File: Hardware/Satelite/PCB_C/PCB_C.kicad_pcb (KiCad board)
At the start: 2 copper layers, 54 x 54 mm, 54 parts, among them IC4 MS563702BA03-50, IC5 BMX055, J1 SWD, J3 Conector_PCB_B-C, J4 Conector_Expansion_CanSat, J5 USB_B_Micro, M1 Spacer, M2 Spacer, M3 Spacer, U1 TXS0104ERGYR, U2 TCA9802DGKR, U3 W25Q32JVSSIQ, U4 TXS0104ERGYR, U5 BL654, U6 Si7006-A20-IM1, U7 Si7051-A20, Y1 LFXTAL016178

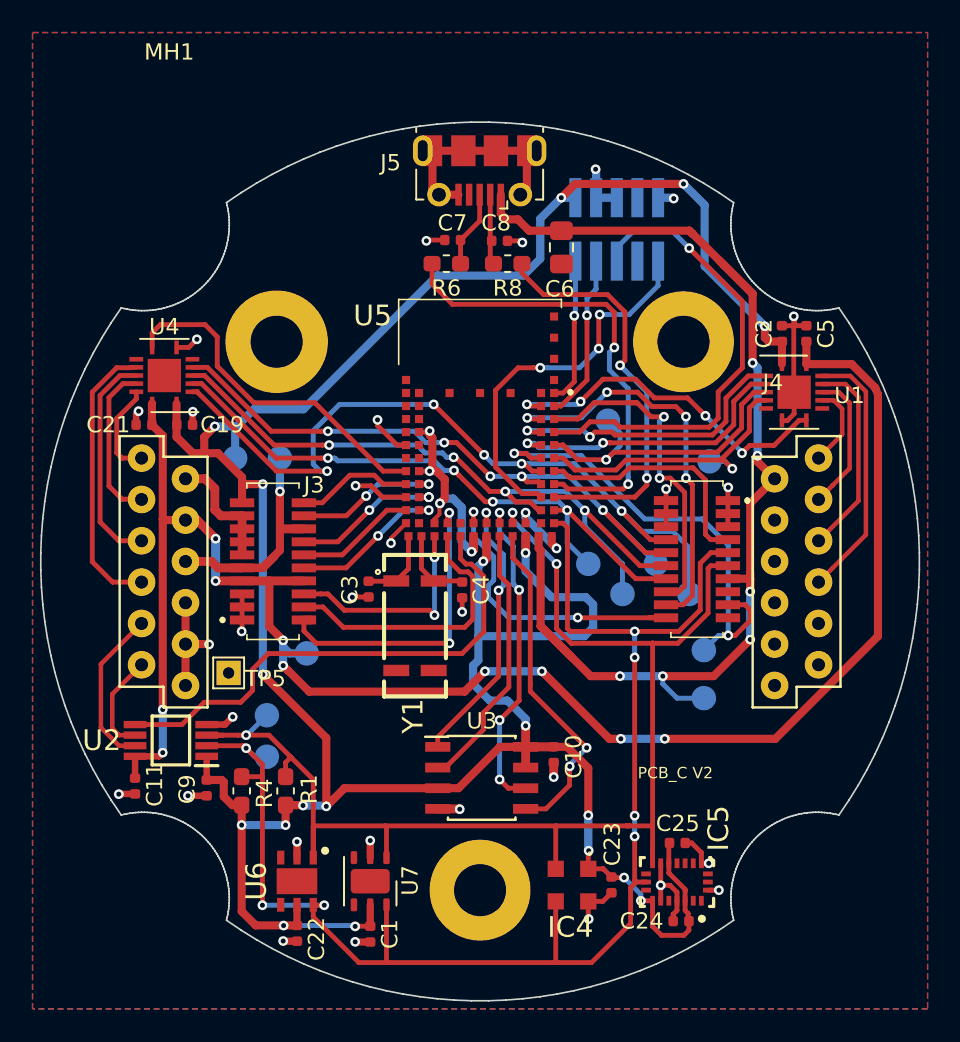
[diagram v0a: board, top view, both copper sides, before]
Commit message: Pequeñas mejoras a PCB_C
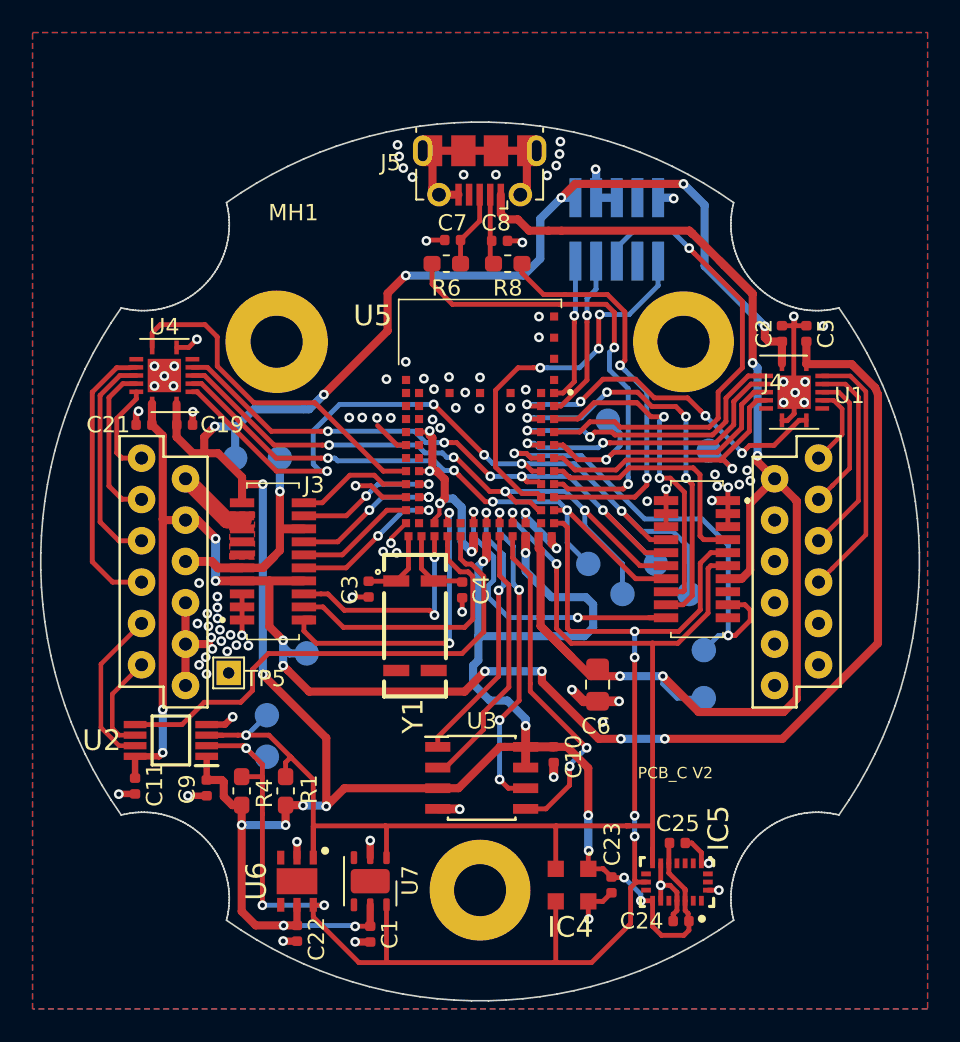
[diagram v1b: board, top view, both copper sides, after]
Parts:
- moved C6 27.0 mm to (17.2, 17.6)
- moved TP10 0.65 mm to (24.1, 3.20)
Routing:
- net VBUS: track 73.4 -> 85.5 mm, vias 6 -> 4
- net +BATT: track 7.58 -> 4.63 mm
- net GND: track 94.0 -> 96.9 mm, vias 36 -> 104
- net +3V3_Internal: track 191.7 -> 193.1 mm, vias 19 -> 21
- net +3V3: track 128.4 -> 129.0 mm
- added copper zone on F.Cu, net +BATT

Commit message: Agregado de modelos 3D a PCB_C
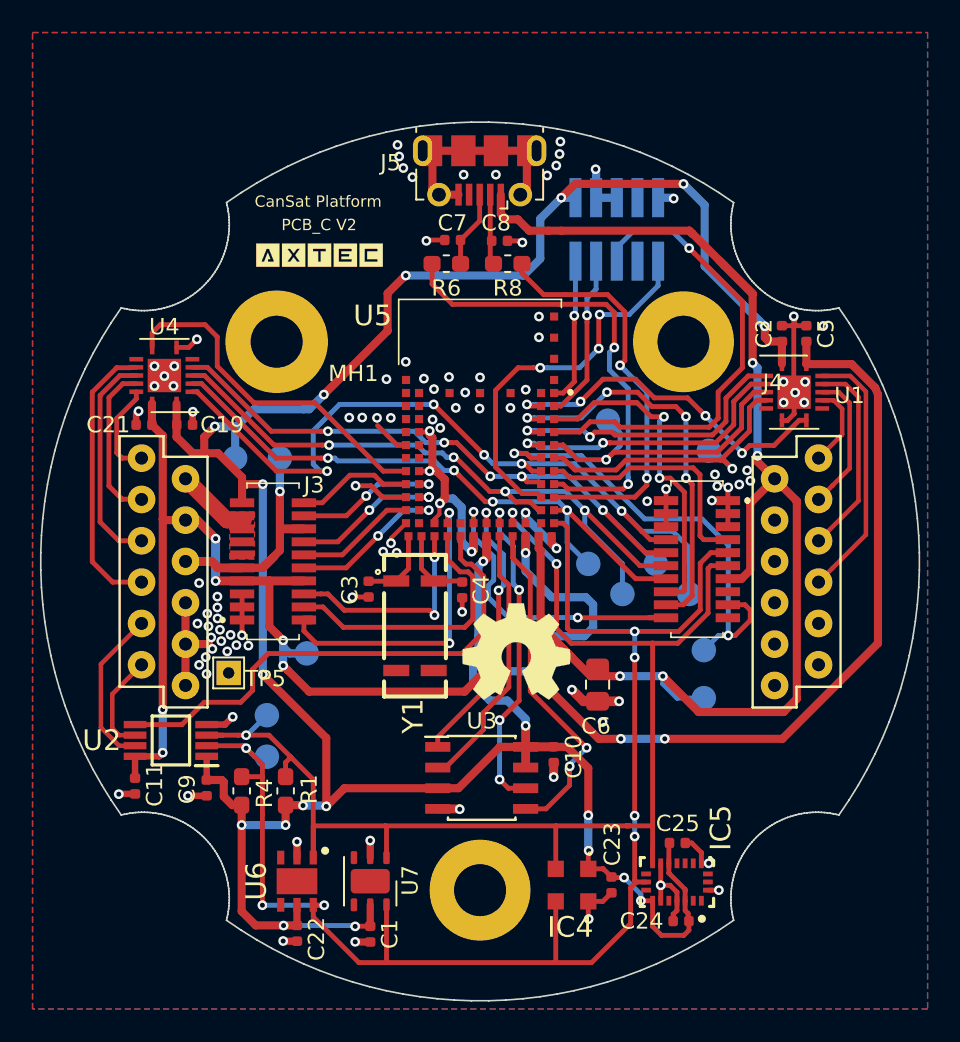
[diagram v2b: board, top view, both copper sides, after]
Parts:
- added G***: LOGO, AXTEC:Logo_AXTEC, B.Cu at (0.05, -9.02)
- added G***: LOGO, AXTEC:Logo_AXTEC, F.Cu at (0.20, -9.02)
- added REF**: OSHW-Symbol_6.7x6mm_SilkScreen, Symbol:OSHW-Symbol_6.7x6mm_SilkScreen, B.Cu at (12.2, 15.5)
- added REF**: OSHW-Symbol_6.7x6mm_SilkScreen, Symbol:OSHW-Symbol_6.7x6mm_SilkScreen, F.Cu at (12.2, 15.5)
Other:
- board text added: "CanSat Platform"

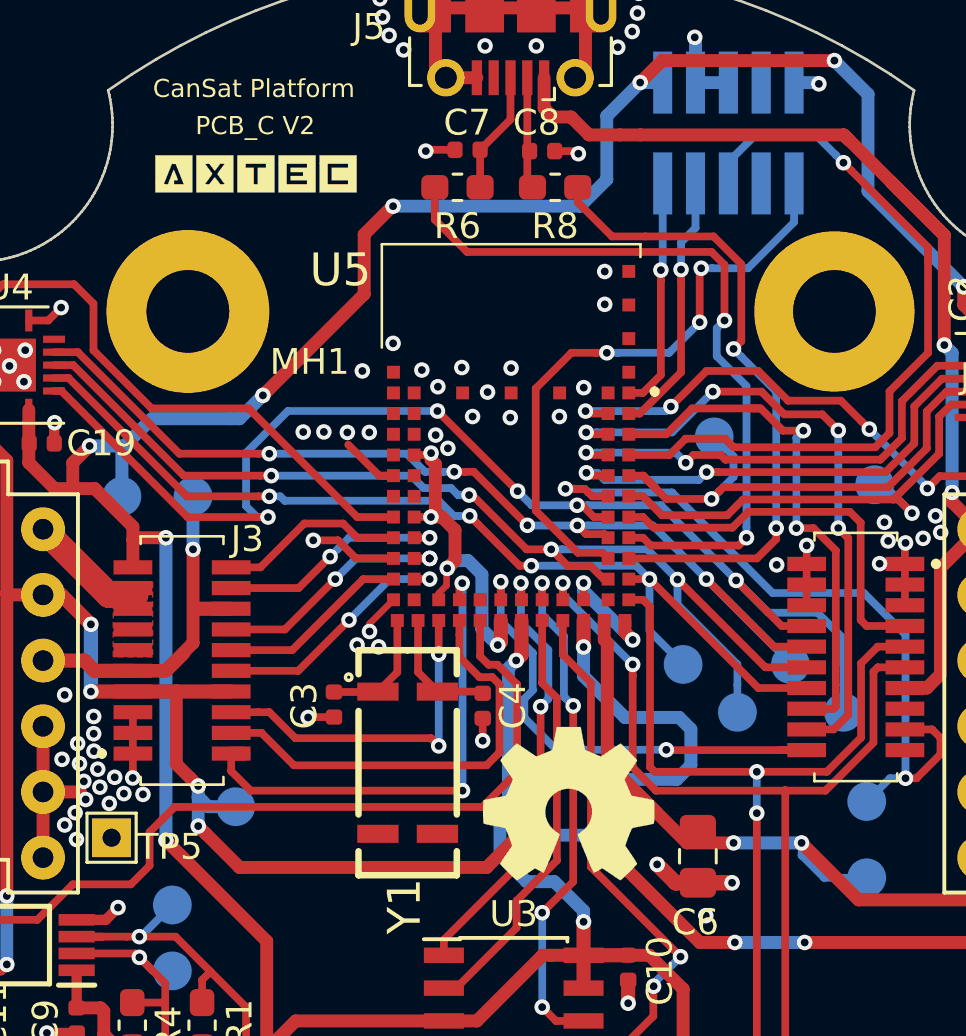
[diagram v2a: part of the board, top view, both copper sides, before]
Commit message: Corrección pin nRST en PCB_C kicad_pcb
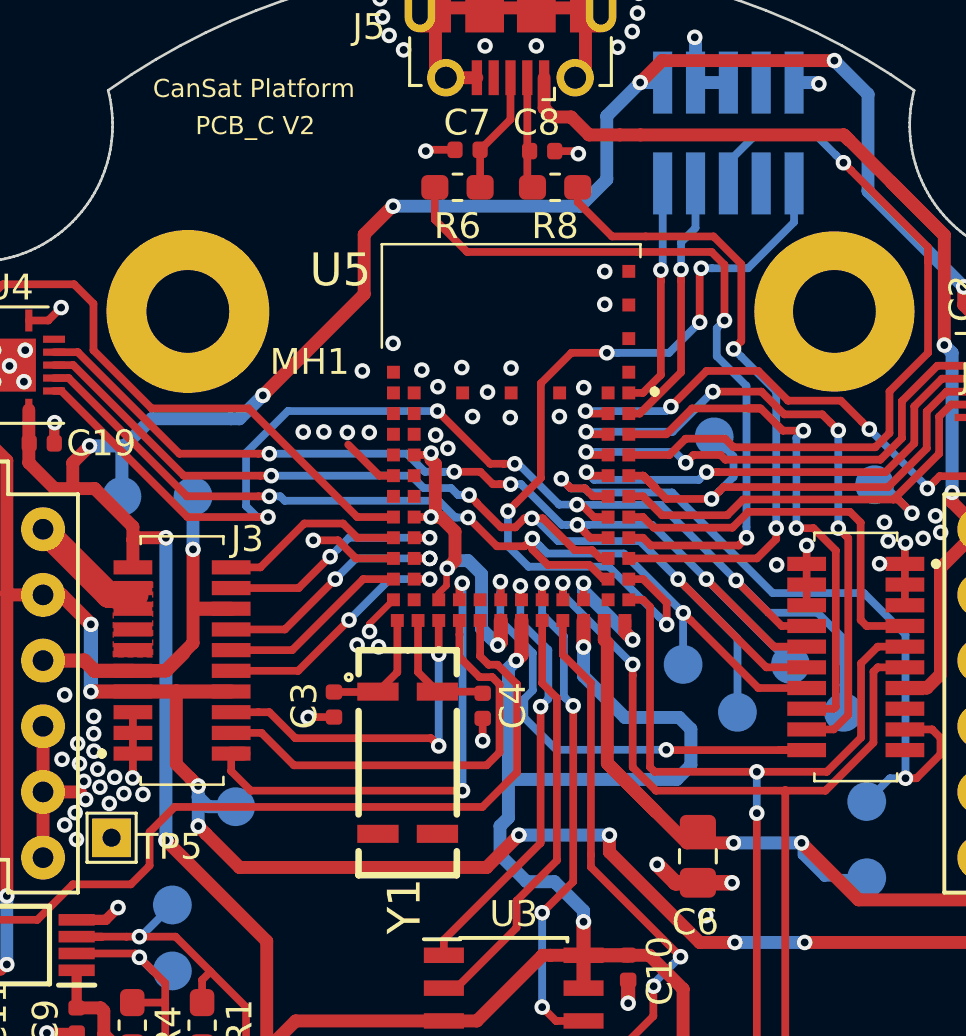
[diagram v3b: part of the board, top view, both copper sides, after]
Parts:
- removed G*** (x2): LOGO, AXTEC:Logo_AXTEC
- removed the REF** at (12.2, 15.5) (x2)
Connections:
- IC5 pad 1: /IMU/ACC_INT -> (no net)
- IC5 pad 10: /IMU/MAG_INT -> (no net)
- IC5 pad 14: /IMU/GYRO_INT -> (no net)
- IC5 pad 15: Net-(IC5-Pad15) -> (no net)
- IC5 pad 16: Net-(IC5-Pad16) -> (no net)
- IC5 pad 18: Net-(IC5-Pad18) -> (no net)
- IC5 pad 19: Net-(IC5-Pad19) -> (no net)
- IC5 pad 2: Net-(IC5-Pad2) -> (no net)
- IC5 pad 5: Net-(IC5-Pad5) -> (no net)
- IC5 pad 8: Net-(IC5-Pad8) -> (no net)
- J1 pad 7: Net-(J1-Pad7) -> (no net)
- J1 pad 8: Net-(J1-Pad8) -> (no net)
- J3 pad 28: Net-(J3-Pad28) -> (no net)
- J3 pad 30: Net-(J3-Pad30) -> (no net)
- J4 pad 10: Net-(J4-Pad10) -> (no net)
- J4 pad 11: Net-(J4-Pad11) -> (no net)
- J4 pad 12: Net-(J4-Pad12) -> (no net)
- J4 pad 5: Net-(J4-Pad5) -> (no net)
- J4 pad 6: Net-(J4-Pad6) -> (no net)
- J4 pad 8: Net-(J4-Pad8) -> (no net)
- J4 pad 9: Net-(J4-Pad9) -> (no net)
- J5 pad 4: Net-(J5-Pad4) -> (no net)
- U1 pad 6: Net-(U1-Pad6) -> (no net)
- U1 pad 9: Net-(U1-Pad9) -> (no net)
- U4 pad 6: Net-(U4-Pad6) -> (no net)
- U4 pad 9: Net-(U4-Pad9) -> (no net)
- U5 pad 18: /nRST -> /SCLK
- U5 pad 19: /SDO -> /nRST
- U5 pad 2: Net-(U5-Pad2) -> (no net)
- U5 pad 20: /SCLK -> /SDO
- U5 pad 22: Net-(U5-Pad22) -> (no net)
- U5 pad 36: Net-(U5-Pad36) -> (no net)
- U5 pad 44: Net-(U5-Pad44) -> (no net)
- U5 pad 53: Net-(U5-Pad53) -> (no net)
- U5 pad 54: Net-(U5-Pad54) -> (no net)
- U5 pad 56: Net-(U5-Pad56) -> (no net)
- U5 pad 57: Net-(U5-Pad57) -> (no net)
- U5 pad 59: Net-(U5-Pad59) -> (no net)
- U5 pad 60: Net-(U5-Pad60) -> (no net)
- U5 pad 61: Net-(U5-Pad61) -> (no net)
- U5 pad 62: Net-(U5-Pad62) -> (no net)
- U5 pad 63: Net-(U5-Pad63) -> (no net)
- U5 pad 64: Net-(U5-Pad64) -> (no net)
- U6 pad 3: Net-(U6-Pad3) -> (no net)
- U6 pad 4: Net-(U6-Pad4) -> (no net)
- U6 pad 7: Net-(U6-Pad7) -> (no net)
- U7 pad 3: Net-(U7-Pad3) -> (no net)
- U7 pad 4: Net-(U7-Pad4) -> (no net)
- Y1 pad 2: Net-(Y1-Pad2) -> (no net)
- Y1 pad 3: Net-(Y1-Pad3) -> (no net)
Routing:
- net /nRST: track 23.6 -> 32.0 mm, vias 3 -> 5
- net /SDO: track 38.7 -> 40.1 mm
- net /SCLK: track 42.7 -> 43.9 mm
- net /CHG: track 28.6 -> 29.2 mm

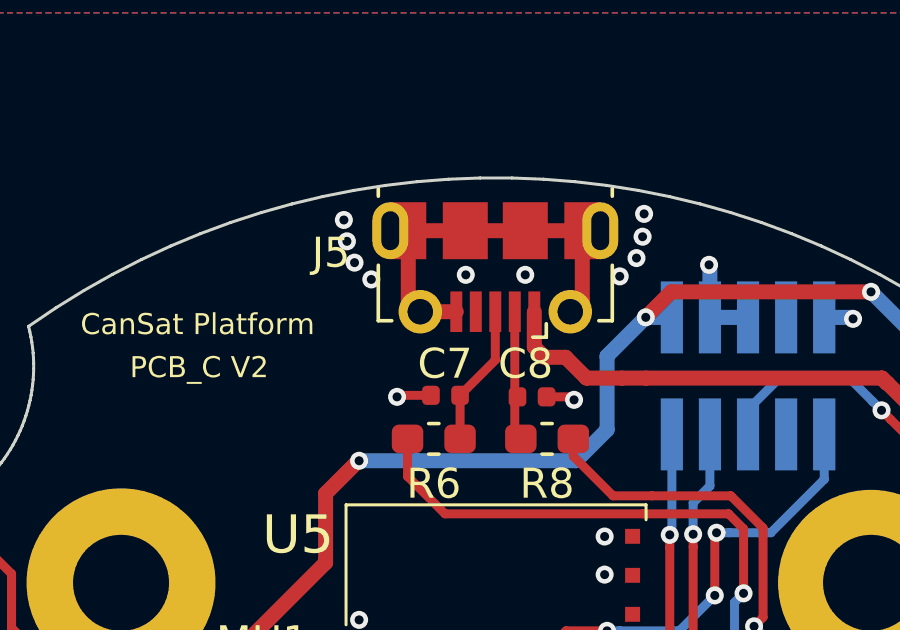
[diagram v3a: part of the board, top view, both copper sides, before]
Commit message: Nuevos conectores micro-usb completamente SMD
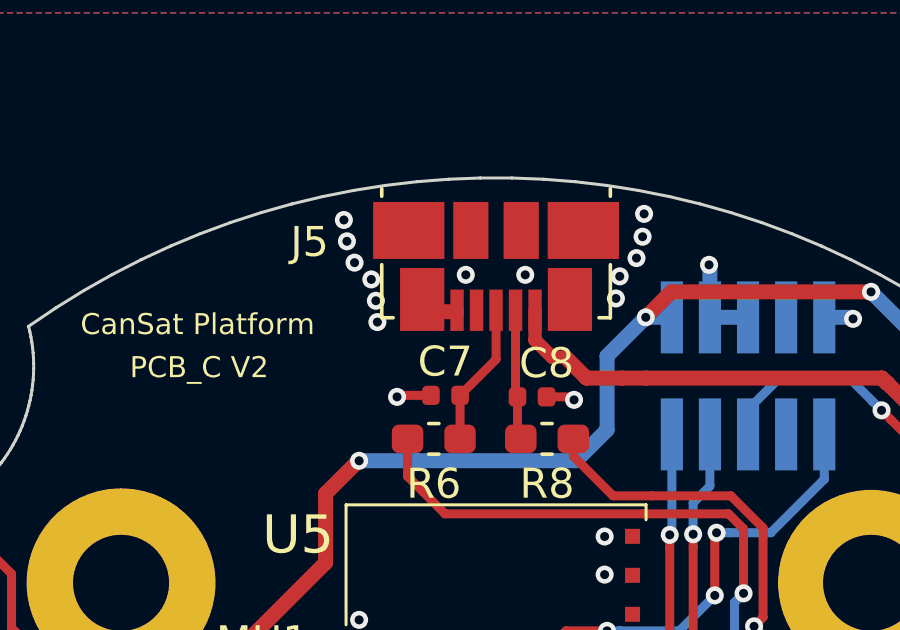
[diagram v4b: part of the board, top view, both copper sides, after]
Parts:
- J5: footprint Connector_USB:USB_Micro-B_Molex-105017-0001 -> Connector_USB:USB_Micro-B_Molex_47346-0001
- moved J5 0.05 mm to (10.0, -14.0)
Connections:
- IC5 pad 1: (no net) -> /IMU/ACC_INT
- IC5 pad 10: (no net) -> /IMU/MAG_INT
- IC5 pad 14: (no net) -> /IMU/GYRO_INT
- IC5 pad 15: (no net) -> Net-(IC5-Pad15)
- IC5 pad 16: (no net) -> Net-(IC5-Pad16)
- IC5 pad 18: (no net) -> Net-(IC5-Pad18)
- IC5 pad 19: (no net) -> Net-(IC5-Pad19)
- IC5 pad 2: (no net) -> Net-(IC5-Pad2)
- IC5 pad 5: (no net) -> Net-(IC5-Pad5)
- IC5 pad 8: (no net) -> Net-(IC5-Pad8)
- J1 pad 7: (no net) -> Net-(J1-Pad7)
- J1 pad 8: (no net) -> Net-(J1-Pad8)
- J3 pad 28: (no net) -> Net-(J3-Pad28)
- J3 pad 30: (no net) -> Net-(J3-Pad30)
- J4 pad 10: (no net) -> Net-(J4-Pad10)
- J4 pad 11: (no net) -> Net-(J4-Pad11)
- J4 pad 12: (no net) -> Net-(J4-Pad12)
- J4 pad 5: (no net) -> Net-(J4-Pad5)
- J4 pad 6: (no net) -> Net-(J4-Pad6)
- J4 pad 8: (no net) -> Net-(J4-Pad8)
- J4 pad 9: (no net) -> Net-(J4-Pad9)
- J5 pad 4: (no net) -> Net-(J5-Pad4)
- U1 pad 6: (no net) -> Net-(U1-Pad6)
- U1 pad 9: (no net) -> Net-(U1-Pad9)
- U4 pad 6: (no net) -> Net-(U4-Pad6)
- U4 pad 9: (no net) -> Net-(U4-Pad9)
- U5 pad 2: (no net) -> Net-(U5-Pad2)
- U5 pad 22: (no net) -> Net-(U5-Pad22)
- U5 pad 36: (no net) -> Net-(U5-Pad36)
- U5 pad 44: (no net) -> Net-(U5-Pad44)
- U5 pad 53: (no net) -> Net-(U5-Pad53)
- U5 pad 54: (no net) -> Net-(U5-Pad54)
- U5 pad 56: (no net) -> Net-(U5-Pad56)
- U5 pad 57: (no net) -> Net-(U5-Pad57)
- U5 pad 59: (no net) -> Net-(U5-Pad59)
- U5 pad 60: (no net) -> Net-(U5-Pad60)
- U5 pad 61: (no net) -> Net-(U5-Pad61)
- U5 pad 62: (no net) -> Net-(U5-Pad62)
- U5 pad 63: (no net) -> Net-(U5-Pad63)
- U5 pad 64: (no net) -> Net-(U5-Pad64)
- U6 pad 3: (no net) -> Net-(U6-Pad3)
- U6 pad 4: (no net) -> Net-(U6-Pad4)
- U6 pad 7: (no net) -> Net-(U6-Pad7)
- U7 pad 3: (no net) -> Net-(U7-Pad3)
- U7 pad 4: (no net) -> Net-(U7-Pad4)
- Y1 pad 2: (no net) -> Net-(Y1-Pad2)
- Y1 pad 3: (no net) -> Net-(Y1-Pad3)
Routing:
- net GND: track 96.8 -> 85.8 mm, vias 104 -> 107

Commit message: Agregado de logos faltantes en PCB_C
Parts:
- added G***: LOGO, AXTEC:Logo_AXTEC, B.Cu at (0.61, -8.51)
- added G***: LOGO, AXTEC:Logo_AXTEC, F.Cu at (0.74, -8.53)
- added REF**: OSHW-Symbol_6.7x6mm_SilkScreen, Symbol:OSHW-Symbol_6.7x6mm_SilkScreen, B.Cu at (12.2, 15.7)
- added REF**: OSHW-Symbol_6.7x6mm_SilkScreen, Symbol:OSHW-Symbol_6.7x6mm_SilkScreen, F.Cu at (12.2, 15.7)
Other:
- board text added: "PCB_C v2.0"
- board text removed: "PCB_C V2"
